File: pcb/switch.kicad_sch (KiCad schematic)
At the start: 4 parts, among them U5 TMR2617

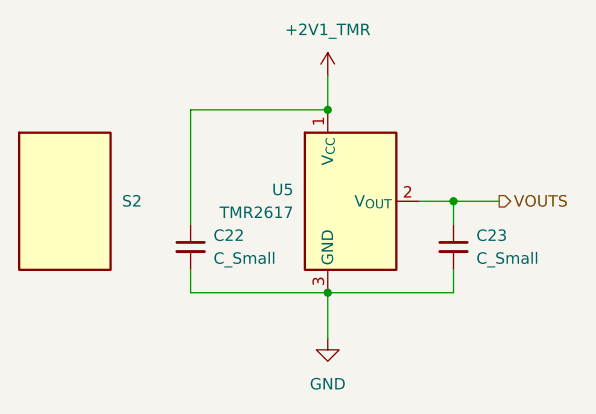
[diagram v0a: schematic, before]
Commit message: A  notes/bypasscaps A  notes/keytravel M  notes/leds A  notes/muxadc M  notes/notes A  notes/pulldown M  notes/scan A  notes/swupdate M  pcb/LED.kicad_sch M  pcb/pcb.kicad_pcb M  pcb/pcb.kicad_prl M  pcb/pcb.kicad_pro M  pcb/pcb.kicad_sch M  pcb/switch.kicad_sch M  placefp.py A  tmr-footprints/C_0402_1005Metric.kicad_mod M  tmr-footprints/C_0603_1608Metric.kicad_mod D  tmr-footprints/C_1206_3216Metric.kicad_mod A  tmr-footprints/Ezurio_BL54L15_Module.kicad_mod A  tmr-footprints/LED_1206_3216Metric_ReverseMount_Hole2.1mm.kicad_mod A  tmr-footprints/Murata_DFE201210U.kicad_mod A  tmr-footprints/R_0402_1005Metric.kicad_mod M  tmr-footprints/SOT-23-3.kicad_mod M  tmr-symbols.kicad_sym
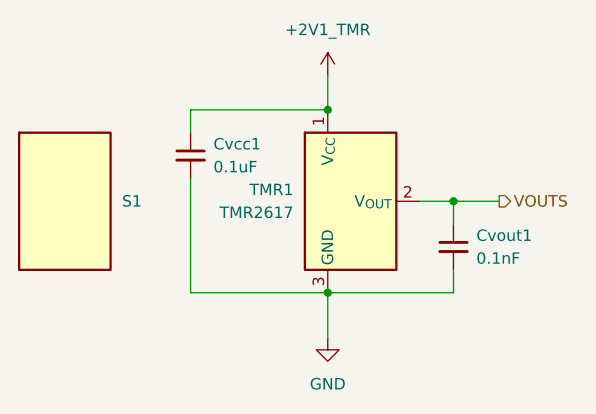
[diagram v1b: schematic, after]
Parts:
- removed U5: TMR2617, tmr-lib:SOT-23-3, symbol tmr-lib:TMR2617
- added TMR1: TMR2617, tmr-lib:SOT-23-3, symbol tmr-lib:TMR2617
- Cvcc1: renamed from C22; value C_Small -> 0.1uF; footprint (none) -> tmr-lib:C_0402_1005Metric
- Cvout1: renamed from C23; value C_Small -> 0.1nF; footprint (none) -> tmr-lib:C_0402_1005Metric
- renumbered S2 to S1
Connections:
- net +2V1_TMR: now also TMR1.1 (V_{CC})
- net GND: now also TMR1.3 (GND)
- net VOUTS: now also TMR1.2 (V_{OUT})
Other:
- moved on the sheet: Cvcc1

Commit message: D  notes/analog D  notes/bypasscaps D  notes/charging D  notes/fusion D  notes/is31fl3731 D  notes/keyfrequency D  notes/keytravel D  notes/leds D  notes/loadsw D  notes/muxadc D  notes/notes D  notes/nrf D  notes/nuts D  notes/parts D  notes/pulldown D  notes/scan D  notes/soldering D  notes/spi D  notes/swupdate D  notes/tmr M  pcb/pcb.kicad_pro M  pcb/pcb.kicad_sch M  pcb/switch.kicad_sch A  tmr-footprints/tps22997.kicad_mod M  tmr-symbols.kicad_sym
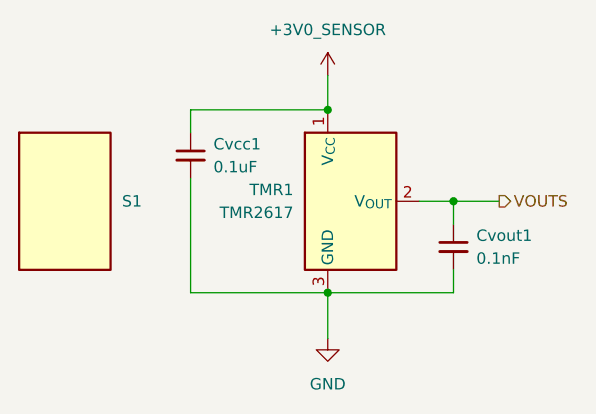
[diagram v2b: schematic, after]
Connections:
- net +2V1_TMR renamed +3V0_SENSOR

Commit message: M  pcb/pcb.kicad_pcb M  pcb/pcb.kicad_sch M  pcb/switch.kicad_sch M  placefp.py A  tmr-footprints/Texas_DYY0016A_TSOT-23-16_2x4.2mm_P0.5mm.kicad_mod M  tmr-symbols.kicad_sym
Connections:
- net +3V0_SENSOR renamed VCCS
